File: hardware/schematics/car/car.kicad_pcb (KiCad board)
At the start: 12 copper layers, 53.3 x 105.2 mm, 21 parts, among them M1 Motor_Servo, Q1 PMOS, SW1 SW_SPST, SW2 SW_Push, SW3 SW_Push, U1 VL53L0CXV0DH1, U10 Mini-560, U11 JGA25-37x, U2 VL53L0CXV0DH1, U3 VL53L0CXV0DH1, U4 Pixy2, U6 TB6612FNG, U7 SparkFun OTOS, U9 Mini-360

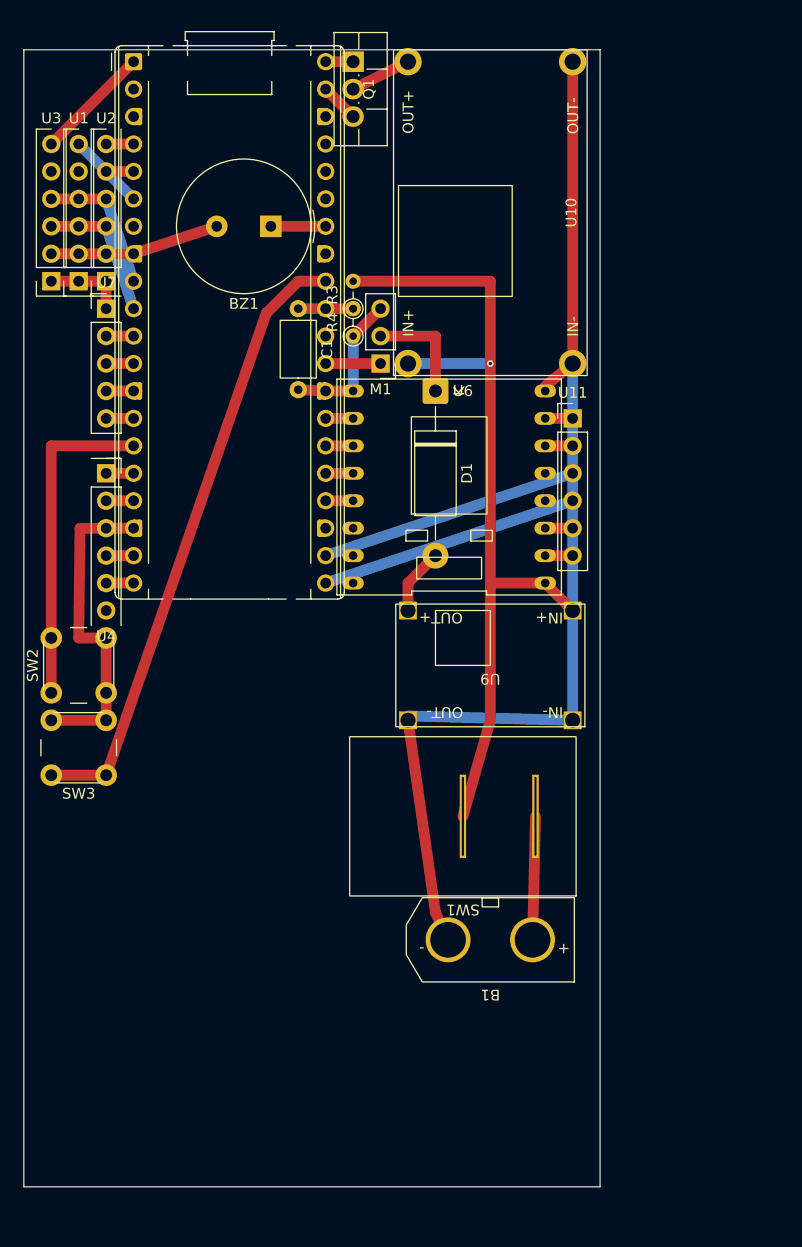
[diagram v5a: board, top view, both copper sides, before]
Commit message: [Schematic] Minor movements
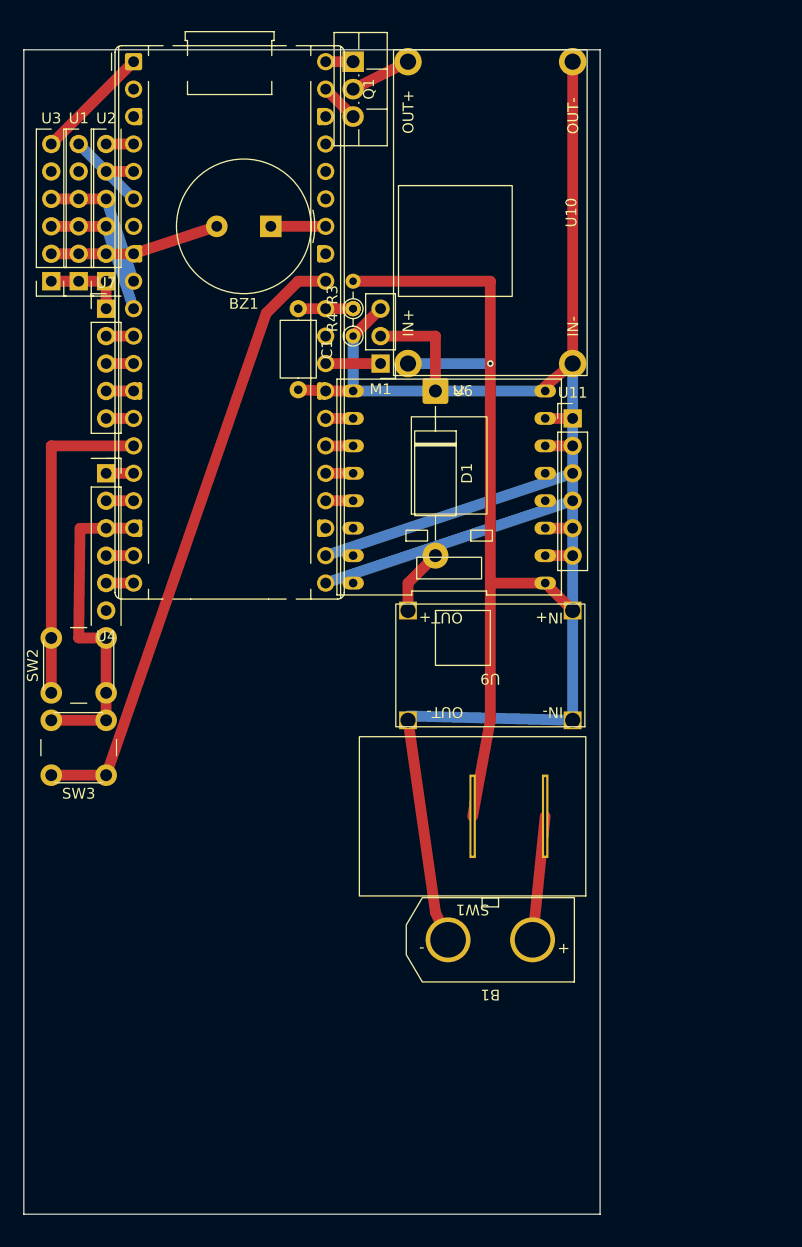
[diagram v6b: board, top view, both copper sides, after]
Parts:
- moved SW1 0.90 mm to (158.4, 85.1)
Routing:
- net GND: track 318.4 -> 336.2 mm
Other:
- board size 53.3 x 105.2 mm -> 53.3 x 107.8 mm
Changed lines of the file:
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@@
 	(footprint "xlnc-foot:SW_SPST_20.96mmx14.74mm"
 		(layer "F.Cu")
-		(at 157.48 85.09 180)
+		(at 158.3775 85.09 180)
 		(property "Reference" "SW1"
 			(at 0 -8.636 180)
@@
 	(gr_rect
 		(start 116.84 14.135)
-		(end 170.18 119.38)
+		(end 170.18 121.92)
 		(stroke
 			(width 0.05)
@@
 	)
 	(segment
+		(start 165.1 45.72)
+		(end 147.32 45.72)
+		(width 1)
+		(layer "B.Cu")
+		(net "GND")
+	)
+	(segment
 		(start 167.64 76.2)
 		(end 152.4 75.8)
@@
 	)
 	(segment
-		(start 160.02 76.2)
-		(end 157.48 85.09)
+		(start 160.02 63.5)
+		(end 165.1 63.5)
 		(width 1)
 		(layer "F.Cu")
@@
 	)
 	(segment
-		(start 160.02 63.5)
-		(end 165.1 63.5)
+		(start 158.3775 85.09)
+		(end 160.02 76.2)
 		(width 1)
 		(layer "F.Cu")
@@
 	(segment
 		(start 163.93 96.52)
-		(end 164.2 85.09)
+		(end 165.0975 85.09)
 		(width 1)
 		(layer "F.Cu")

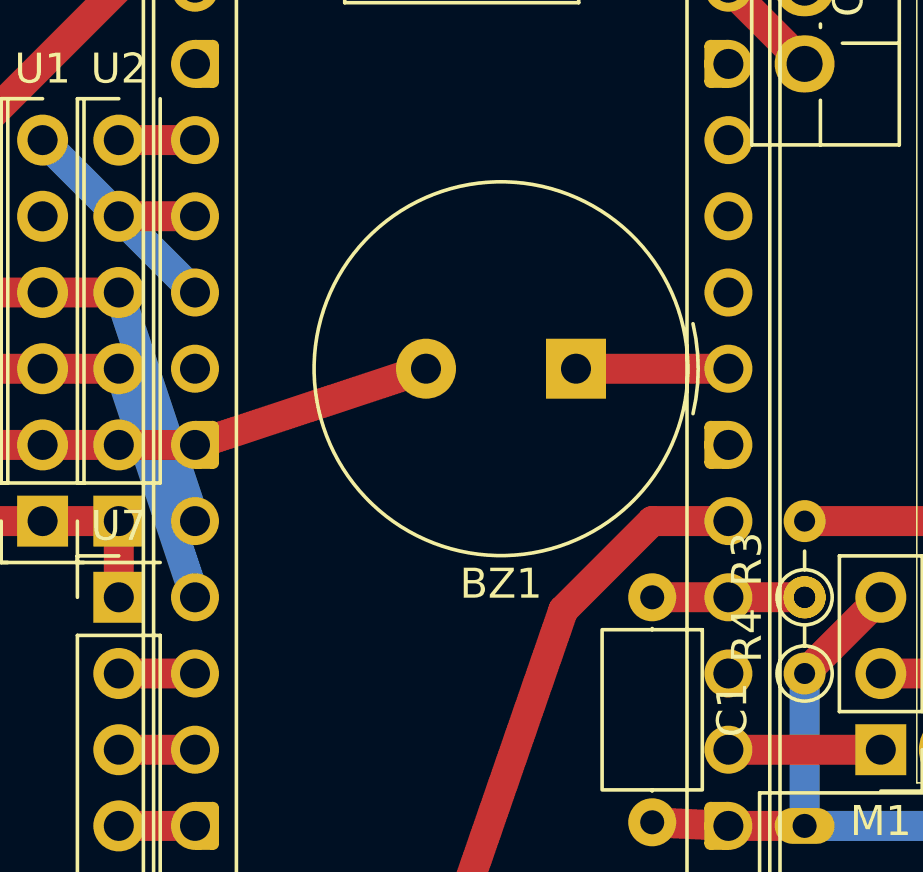
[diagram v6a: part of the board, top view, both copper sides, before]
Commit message: [Schematic] Add 200ohm R in series with buzzer to limit current.
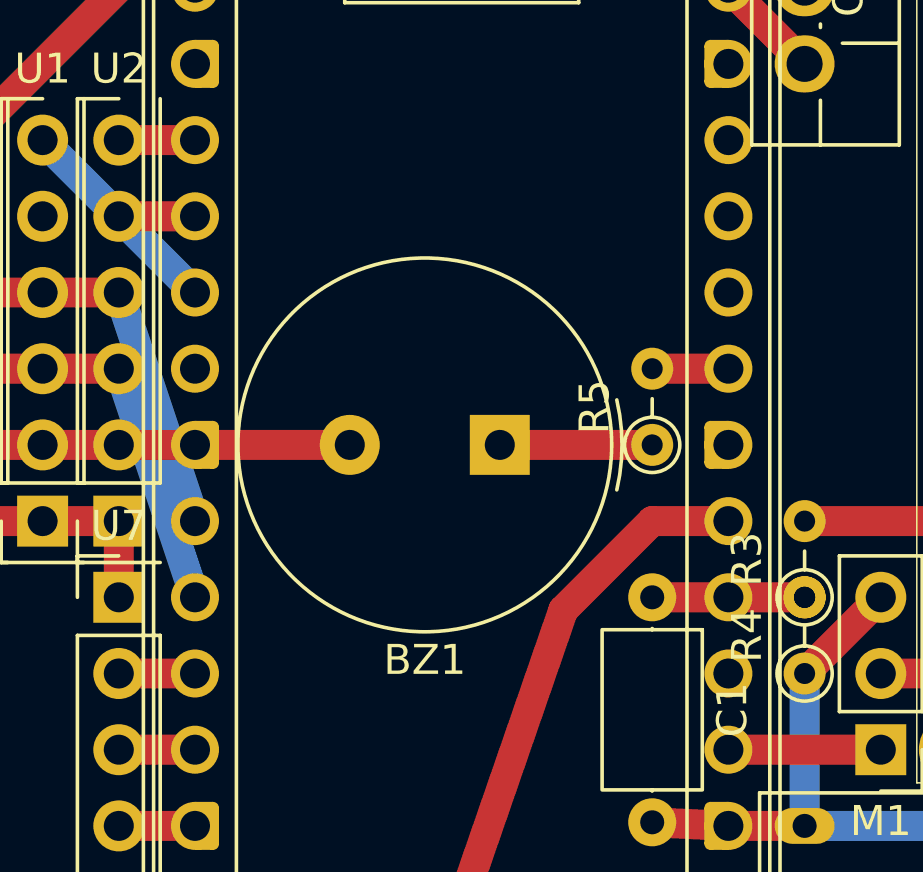
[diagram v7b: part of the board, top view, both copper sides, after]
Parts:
- added R5: 200, Resistor_THT:R_Axial_DIN0204_L3.6mm_D1.6mm_P2.54mm_Vertical, F.Cu at (142.2, 33.0)
- moved BZ1 3.59 mm to (137.2, 33.0)
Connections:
- BZ1 pad 1: Net-(A1-GPIO28_ADC2) -> Net-(BZ1-+)
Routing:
- net Net-(BZ1-+): track 0.00 -> 5.08 mm
- net GND: track 336.2 -> 333.3 mm
- net Net-(A1-GPIO28_ADC2): track 5.08 -> 2.54 mm
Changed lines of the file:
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@@
 		(sheetname "/")
 		(sheetfile "car.kicad_sch")
+		(units
+			(unit
+				(name "A")
+				(pins "1" "2" "3" "4")
+			)
+		)
 		(attr smd)
 		(duplicate_pad_numbers_are_jumpers no)
@@
 		(embedded_fonts no)
 	)
+	(footprint "Resistor_THT:R_Axial_DIN0204_L3.6mm_D1.6mm_P2.54mm_Vertical"
+		(layer "F.Cu")
+		(at 142.24 33.02 90)
+		(descr "Resistor, Axial_DIN0204 series, Axial, Vertical, pin pitch=2.54mm, 0.167W, length*diameter=3.6*1.6mm^2, http://cdn-reichelt.de/documents/datenblatt/B400/1_4W%23YAG.pdf")
+		(tags "Resistor Axial_DIN0204 series Axial Vertical pin pitch 2.54mm 0.167W length 3.6mm diameter 1.6mm")
+		(property "Reference" "R5"
+			(at 1.27 -1.92 90)
+			(layer "F.SilkS")
+			(effects
+				(font
+					(size 1 1)
+					(thickness 0.15)
+				)
+			)
+		)
+		(property "Value" "200"
+			(at 1.27 1.92 90)
+			(layer "F.Fab")
+			(effects
+				(font
+					(size 1 1)
+					(thickness 0.15)
+				)
+			)
+		)
+		(property "Datasheet" ""
+			(at 0 0 90)
+			(layer "F.Fab")
+			(hide yes)
+			(effects
+				(font
+					(size 1.27 1.27)
+				)
+			)
+		)
+		(property "Description" "Resistor"
+			(at 0 0 90)
+			(layer "F.Fab")
+			(hide yes)
+			(effects
+				(font
+					(size 1.27 1.27)
+				)
+			)
+		)
+		(property ki_fp_filters "R_*")
+		(sheetname "/")
+		(sheetfile "car.kicad_sch")
+		(units
+			(unit
+				(name "A")
+				(pins "1" "2")
+			)
+		)
+		(attr through_hole)
+		(duplicate_pad_numbers_are_jumpers no)
+		(fp_line
+			(start 0.92 0)
+			(end 1.54 0)
+			(stroke
+				(width 0.12)
+				(type solid)
+			)
+			(layer "F.SilkS")
+		)
+		(fp_circle
+			(center 0 0)
+			(end 0.92 0)
+			(stroke
+				(width 0.12)
+				(type solid)
+			)
+			(fill no)
+			(layer "F.SilkS")
+		)
+		(fp_rect
+			(start -1.05 -1.05)
+			(end 3.49 1.05)
+			(stroke
+				(width 0.05)
+				(type solid)
+			)
+			(fill no)
+			(layer "F.CrtYd")
+		)
+		(fp_line
+			(start 0 0)
+			(end 2.54 0)
+			(stroke
+				(width 0.1)
+				(type solid)
+			)
+			(layer "F.Fab")
+		)
+		(fp_circle
+			(center 0 0)
+			(end 0.8 0)
+			(stroke
+				(width 0.1)
+				(type solid)
+			)
+			(fill no)
+			(layer "F.Fab")
+		)
+		(fp_text user "${REFERENCE}"
+			(at 1.27 -1.92 90)
+			(layer "F.Fab")
+			(effects
+				(font
+					(size 1 1)
+					(thickness 0.15)
+				)
+			)
+		)
+		(pad "1" thru_hole circle
+			(at 0 0 90)
+			(size 1.4 1.4)
+			(drill 0.7)
+			(layers "*.Cu" "*.Mask")
+			(remove_unused_layers no)
+			(net "Net-(BZ1-+)")
+			(pintype "passive")
+		)
+		(pad "2" thru_hole circle
+			(at 2.54 0 90)
+			(size 1.4 1.4)
+			(drill 0.7)
+			(layers "*.Cu" "*.Mask")
+			(remove_unused_layers no)
+			(net "Net-(A1-GPIO28_ADC2)")
+			(pintype "passive")
+		)
+		(embedded_fonts no)
+		(model "${KICAD10_3DMODEL_DIR}/Resistor_THT.3dshapes/R_Axial_DIN0204_L3.6mm_D1.6mm_P2.54mm_Vertical.step"
+			(offset
+				(xyz 0 0 0)
+			)
+			(scale
+				(xyz 1 1 1)
+			)
+			(rotate
+				(xyz 0 0 0)
+			)
+		)
+	)
 	(footprint "xlnc-foot:SW_SPST_20.96mmx14.74mm"
 		(layer "F.Cu")
@@
 			)
 		)
-		(property "Description" ""
+		(property "Description" "Push button switch, generic, two pins"
 			(at 0 0 90)
 			(unlocked yes)
@@
 		(sheetname "/")
 		(sheetfile "car.kicad_sch")
+		(units
+			(unit
+				(name "A")
+				(pins "1" "2")
+			)
+		)
 		(attr through_hole)
 		(duplicate_pad_numbers_are_jumpers no)
@@
 		(sheetname "/")
 		(sheetfile "car.kicad_sch")
+		(units
+			(unit
+				(name "A")
+				(pins "1" "2" "3" "4")
+			)
+		)
 		(attr smd)
 		(duplicate_pad_numbers_are_jumpers no)
@@
 	(footprint "Buzzer_Beeper:Buzzer_TDK_PS1240P02BT_D12.2mm_H6.5mm"
 		(layer "F.Cu")
-		(at 139.7 30.48 180)
+		(at 137.16 33.02 180)
 		(descr "Buzzer, D12.2mm height 6.5mm, https://product.tdk.com/info/en/catalog/datasheets/piezoelectronic_buzzer_ps_en.pdf")
 		(tags "buzzer")
@@
 			(layers "*.Cu" "*.Mask")
 			(remove_unused_layers no)
-			(net "Net-(A1-GPIO28_ADC2)")
+			(net "Net-(BZ1-+)")
 			(pinfunction "+_1")
 			(pintype "passive")
@@
 			)
 		)
-		(property "Description" ""
+		(property "Description" "Push button switch, generic, two pins"
 			(at 0 0 180)
 			(unlocked yes)
@@
 		(sheetname "/")
 		(sheetfile "car.kicad_sch")
+		(units
+			(unit
+				(name "A")
+				(pins "1" "2")
+			)
+		)
 		(attr through_hole)
 		(duplicate_pad_numbers_are_jumpers no)
@@
 	)
 	(segment
+		(start 132.16 33.02)
+		(end 127 33.02)
+		(width 1)
+		(layer "F.Cu")
+		(net "GND")
+	)
+	(segment
 		(start 149.86 38.1)
 		(end 147.32 40.64)
@@
 	)
 	(segment
-		(start 134.7 30.48)
-		(end 127 33.02)
-		(width 1)
-		(layer "F.Cu")
-		(net "GND")
-	)
-	(segment
 		(start 165.1 58.42)
 		(end 167.64 58.42)
@@
 	)
 	(segment
-		(start 139.7 30.48)
+		(start 142.24 30.48)
 		(end 144.78 30.48)
 		(width 1)
@@
 		(net "Net-(D1-K)")
 	)
+	(segment
+		(start 137.16 33.02)
+		(end 142.24 33.02)
+		(width 1)
+		(layer "F.Cu")
+		(net "Net-(BZ1-+)")
+	)
 	(group ""
